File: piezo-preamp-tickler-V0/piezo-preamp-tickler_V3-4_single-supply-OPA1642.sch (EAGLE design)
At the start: 60 parts, among them IC1 OPA1642, J1 Battery, Q1 BQ21040, Q2 MMBFJ201, Q5 BQ297X, Q7 DMN2400, SW1 SPDT, SW2-SPST INPUT-select

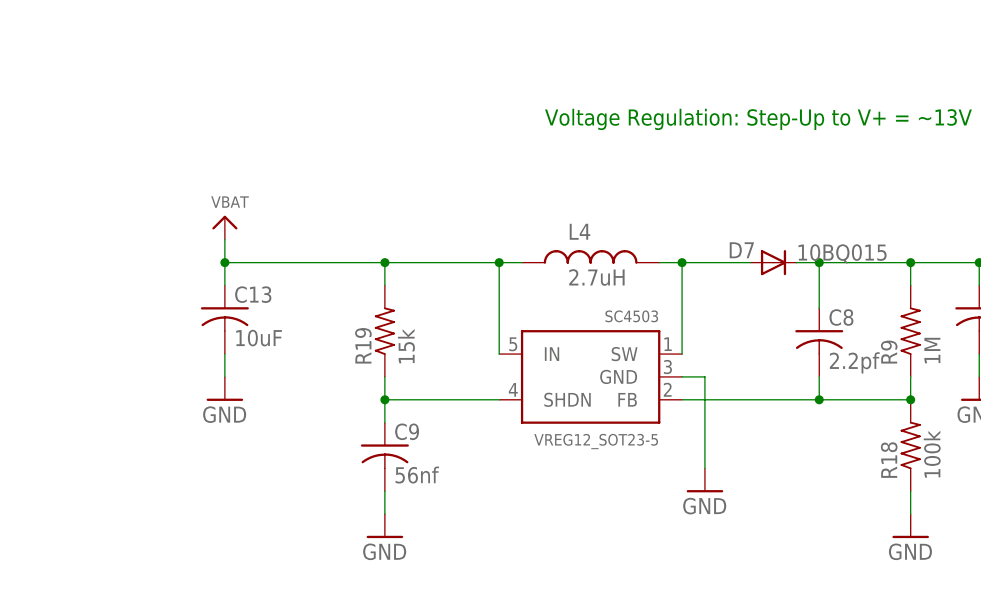
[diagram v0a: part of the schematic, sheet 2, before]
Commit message: updates to piezo preamp
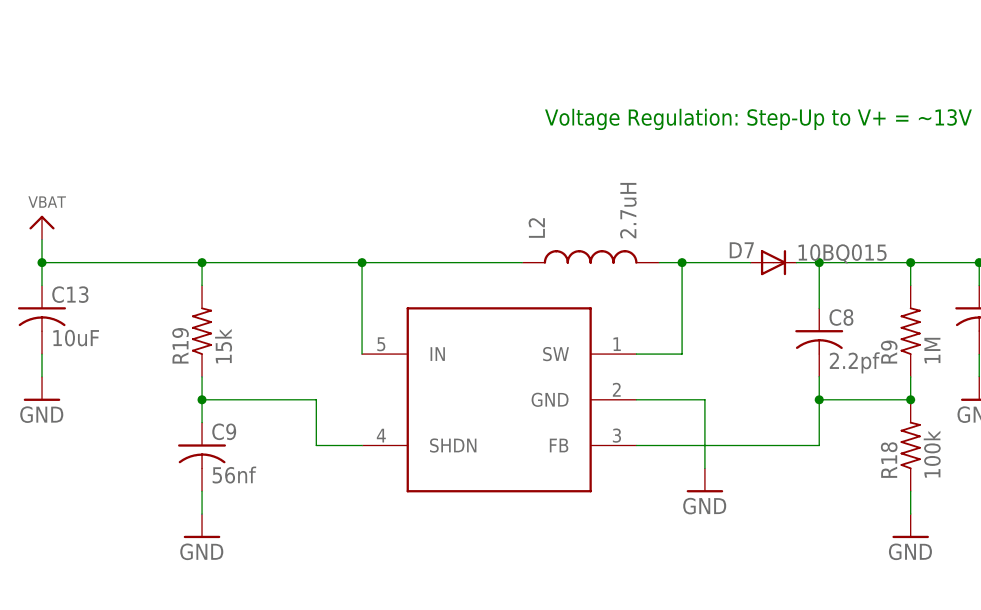
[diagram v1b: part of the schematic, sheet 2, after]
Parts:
- removed D1, D2: (no value), diode:DIODE-SOD123
- removed L4: 2.7uH, SparkFun:INDUCTORCR54
- removed SC4503: VREG12_SOT23-5, CMU-ArtFab:VREG12_SOT23-5
- removed TO-HEADSET, TO-PHONE, TO-PHONE1: AUDIO-JACK3LGPADS, Daniel:AUDIO-JACK3LGPADS
- added J$1: Phone, CMU-ArtFab:TRRS-3.5MMLGPADS
- added J$2: Headphones, CMU-ArtFab:TRRS-3.5MMLGPADS
- added L2: 2.7uH, SparkFun-Passives:INDUCTORCR54
- added Q3: SC4503, CMU-ArtFab:SC4503
- added U$1: Mixer, CMU-ArtFab:TRS-1/8"-3.5MM
- C1: device adafruit:C-USC0603 -> adafruit:C-USC0805
- C13, C14, C8, C9: device adafruit:C-USC0805 -> adafruit:C-USC0603
- renumbered Q5 to IC4, Q7 to IC3, U$5 to IC2
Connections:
- removed net N$1: D1.A, D2.A
- net GND: now also J$1.TIP, J$2.TIP, Q3.GND, U$1.SLEEVE; no longer D2.C, SC4503.GND, TO-HEADSET.RING2, TO-PHONE.RING2, TO-PHONE1.EARTH
- net N$10: no longer D1.C
- net N$12: now also U$1.RING1, U$1.TIP; no longer TO-PHONE1.RING1, TO-PHONE1.TIP
- net N$13: now also J$1.RING1, J$2.RING1; no longer TO-HEADSET.TIP, TO-PHONE.TIP
- net N$15: now also J$1.RING2, J$2.RING2; no longer TO-HEADSET.RING1, TO-PHONE.RING1
- net N$17: now also J$1.SLEEVE; no longer TO-PHONE.EARTH
- net N$29: now also Q3.SHDN; no longer SC4503.SHDN
- net N$30: now also Q3.FB; no longer SC4503.FB
- net N$32: now also L2.2, Q3.SW; no longer L4.2, SC4503.SW
- net N$4: now also J$2.SLEEVE; no longer TO-HEADSET.EARTH
- net VBAT: now also L2.1, Q3.IN; no longer L4.1, SC4503.IN
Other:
- moved on the sheet: C13, C9, R19
